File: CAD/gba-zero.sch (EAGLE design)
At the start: 57 parts, among them IC5 APX803, Q2 BSS138, U1 NC7WZ16, U2 LM4875

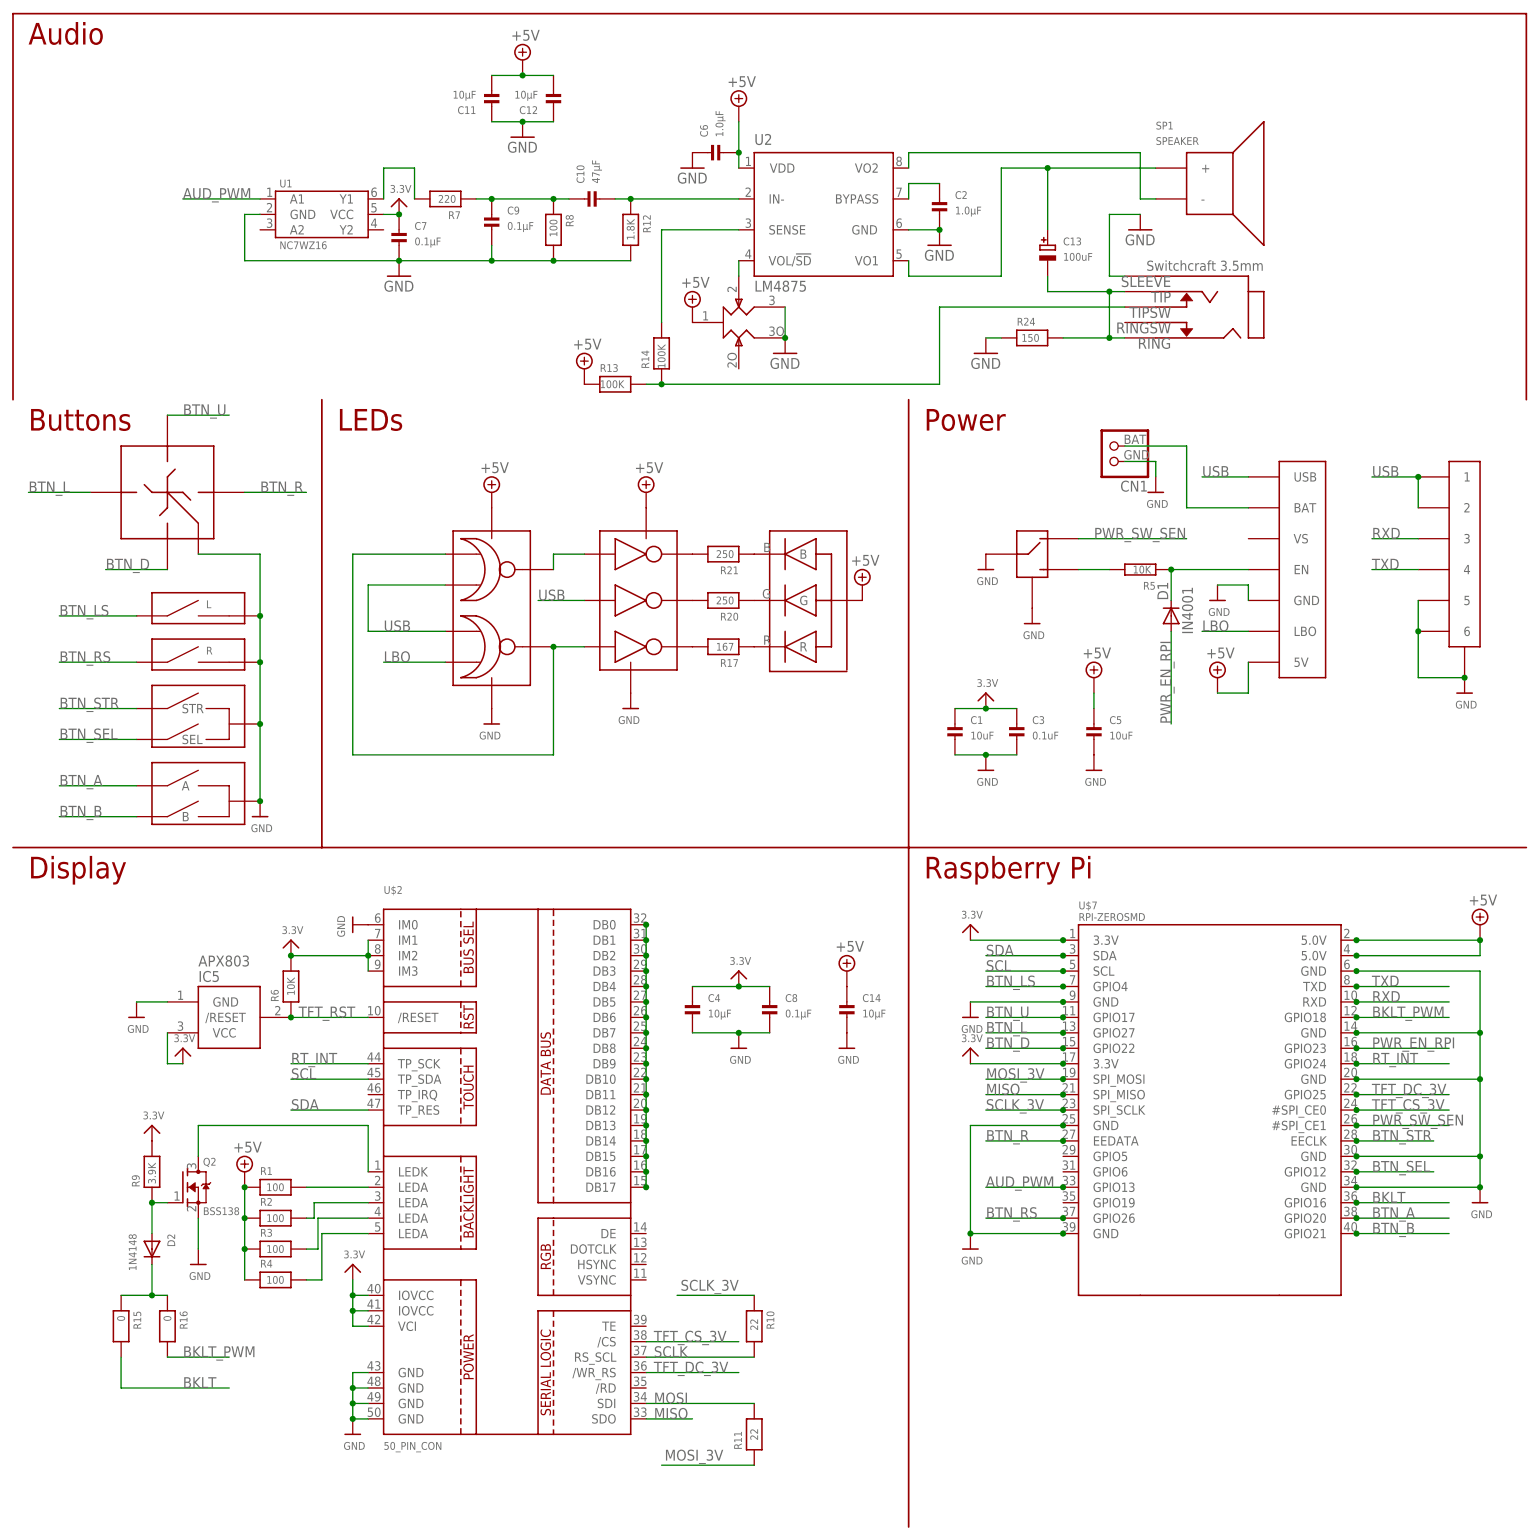
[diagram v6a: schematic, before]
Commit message: Renumbered parts
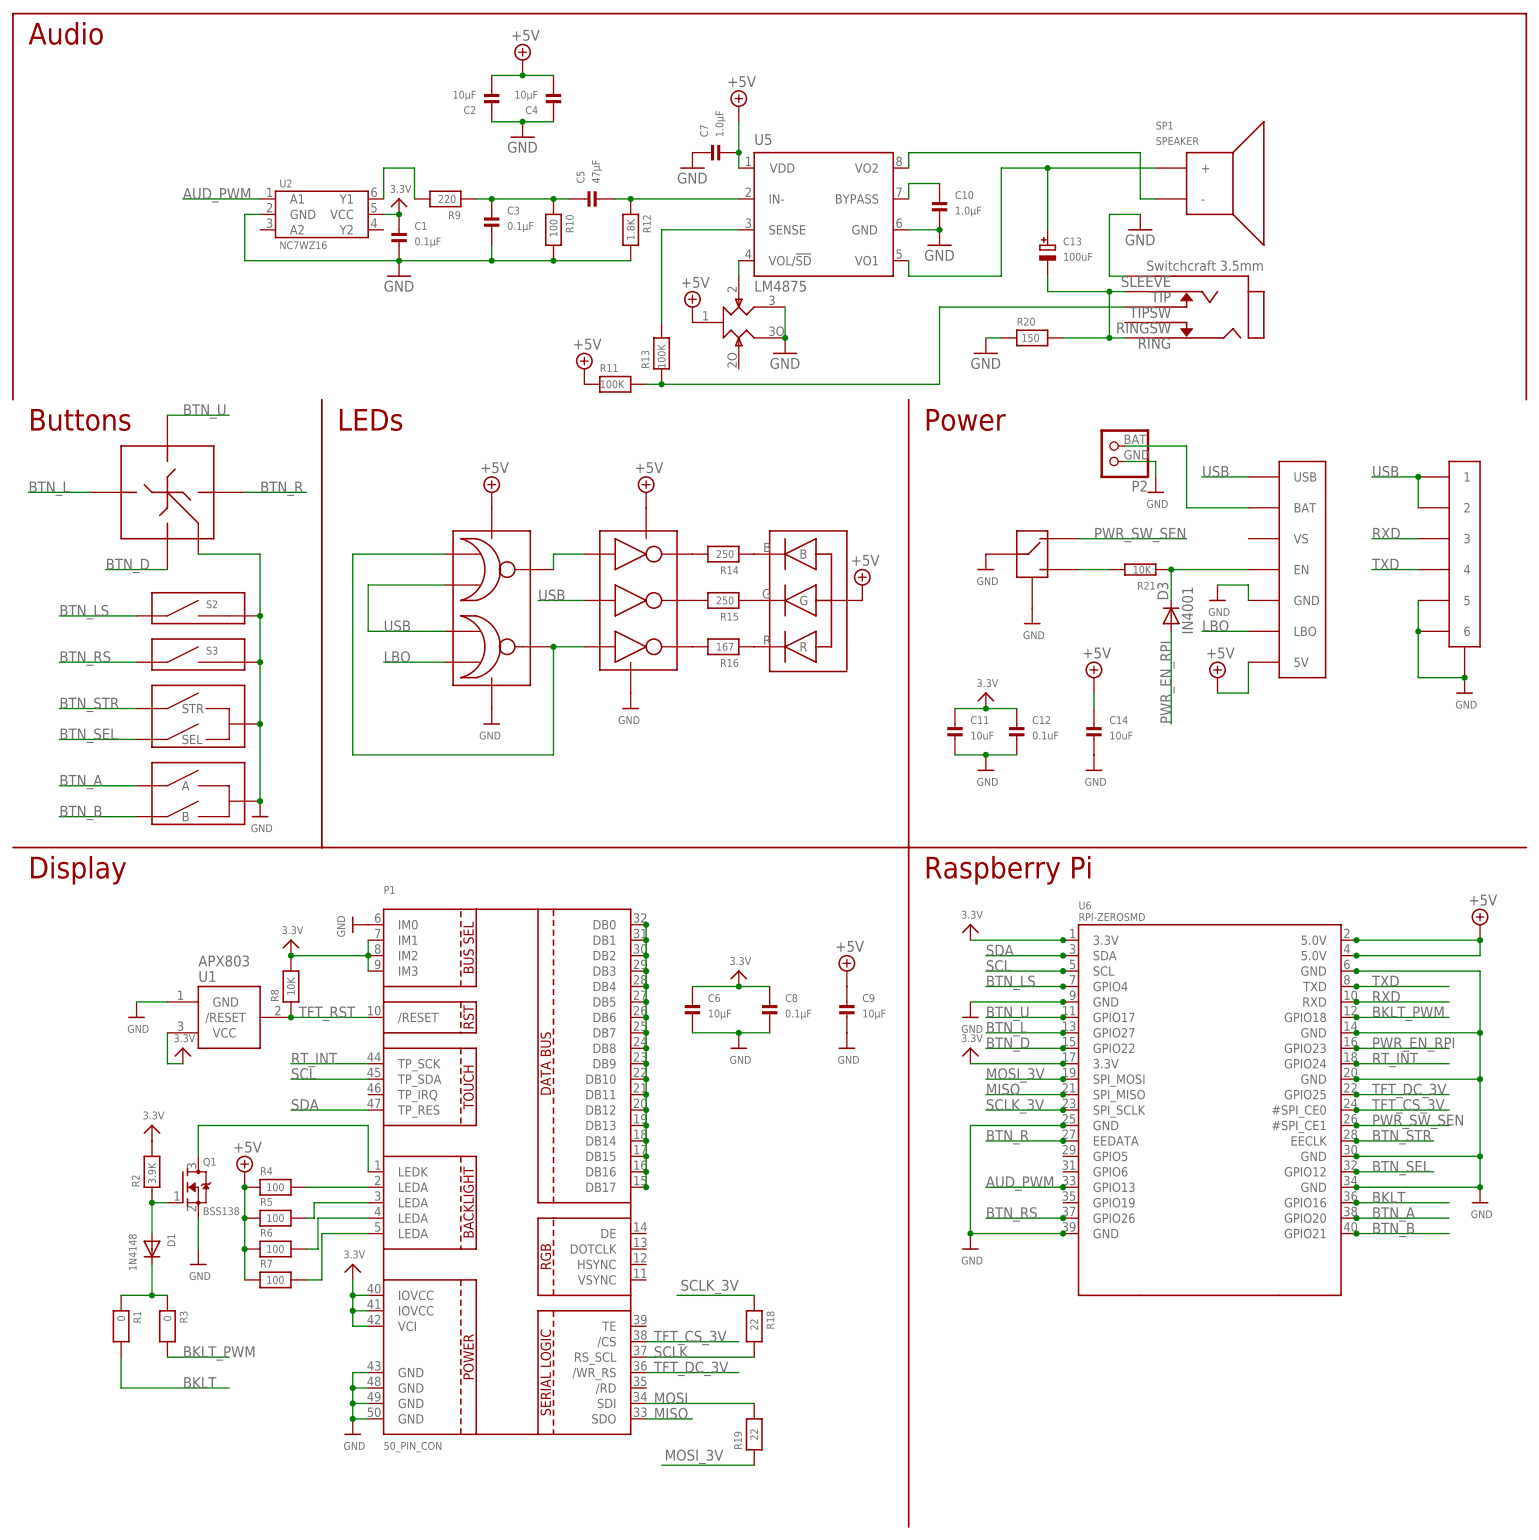
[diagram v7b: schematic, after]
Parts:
- removed IC5: APX803, adafruit:AXP083-SAG
- removed R24: 150, microbuilder:RESISTOR0603
- removed U$17: 10K, gba-zero-parts:RK10J12E0A0A
- removed U$44: LTST-C19HE1WT, gba-zero-parts:LTST-C19HE1WT
- added D3: IN4001, diode:DIODE-D-7.5
- added R18, R19: 22, microbuilder:RESISTOR0805
- added U5: LM4875, gba-zero-parts:LM4875
- C1: value 10uF -> 0.1μF; device microbuilder:CAP_CERAMIC0805 -> microbuilder:CAP_CERAMIC0603
- C10: value 47μF -> 1.0μF
- C11, C14: value 10μF -> 10uF; device microbuilder:CAP_CERAMIC0603 -> microbuilder:CAP_CERAMIC0805
- C12: value 10μF -> 0.1uF; device microbuilder:CAP_CERAMIC0603 -> microbuilder:CAP_CERAMIC0805
- C2, C6: value 1.0μF -> 10μF
- C3: value 0.1uF -> 0.1μF; device microbuilder:CAP_CERAMIC0805 -> microbuilder:CAP_CERAMIC0603
- C5: value 10uF -> 47μF; device microbuilder:CAP_CERAMIC0805 -> microbuilder:CAP_CERAMIC0603
- C7: value 0.1μF -> 1.0μF
- C9: value 0.1μF -> 10μF
- D1: value IN4001 -> 1N4148; device diode:DIODE-D-7.5 -> microbuilder:DIODESOD-323
- D2: value 1N4148 -> LTST-C19HE1WT; device microbuilder:DIODESOD-323 -> gba-zero-parts:LTST-C19HE1WT
- R1, R3: value 100 -> 0; device microbuilder:RESISTOR0805 -> microbuilder:RESISTOR0603
- R10: value 22 -> 100; device microbuilder:RESISTOR0805 -> microbuilder:RESISTOR0603
- R11: value 22 -> 100K; device microbuilder:RESISTOR0805 -> microbuilder:RESISTOR0603
- R14: value 100K -> 250; device microbuilder:RESISTOR0603 -> microbuilder:RESISTOR0805
- R15: value 0 -> 250; device microbuilder:RESISTOR0603 -> microbuilder:RESISTOR0805
- R16: value 0 -> 167; device microbuilder:RESISTOR0603 -> microbuilder:RESISTOR0805
- R17: value 167 -> 10K; device microbuilder:RESISTOR0805 -> gba-zero-parts:RK10J12E0A0A
- R2: value 100 -> 3.9K
- R20: value 250 -> 150; device microbuilder:RESISTOR0805 -> microbuilder:RESISTOR0603
- R21: value 250 -> 10K; device microbuilder:RESISTOR0805 -> resistor:R-EU_0204/7
- R5: value 10K -> 100; device resistor:R-EU_0204/7 -> microbuilder:RESISTOR0805
- R6: value 10K -> 100
- R7: value 220 -> 100; device microbuilder:RESISTOR0603 -> microbuilder:RESISTOR0805
- R8: value 100 -> 10K; device microbuilder:RESISTOR0603 -> microbuilder:RESISTOR0805
- R9: value 3.9K -> 220; device microbuilder:RESISTOR0805 -> microbuilder:RESISTOR0603
- U1: value NC7WZ16 -> APX803; device fairchild:NC7WZ16 -> adafruit:AXP083-SAG
- U2: value LM4875 -> NC7WZ16; device gba-zero-parts:LM4875 -> fairchild:NC7WZ16
- renumbered CN1 to P2, L to S2, Q2 to Q1, R to S3, U$10 to P3, U$11 to S6, U$12 to U7, U$16 to J1, U$18 to S4, U$2 to P1, U$20 to S5, U$3 to S1, U$42 to U3, U$43 to U4, U$7 to U6
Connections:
- net +5V: now also C2.P$2, C4.P$2, C7.P$2, C9.P$1, D2.VCC, R11.1, R17.1, R5.1, R6.1, R7.1, U5.VDD; no longer C11.P$2, C12.P$2, C5.P$1, C6.P$2, R1.1, R13.1, R2.1, R3.1, U$17.1, U$44.VCC, U2.VDD
- net 3.3V: now also C11.P$1, C12.P$1, C6.P$1, R2.2, R8.2, U2.VCC; no longer C3.P$1, C4.P$1, C7.P$1, IC5.VCC, R6.2, R9.2
- net AUD_PWM: now also U2.A1; no longer U1.A1
- net BKLT: now also R1.2; no longer R15.2
- net BKLT_PWM: now also R3.2; no longer R16.2
- net BYPASS: now also C10.P$1, U5.BYPASS; no longer C2.P$1, U2.BYPASS
- net GND: now also C10.P$2, C11.P$2, C12.P$2, C2.P$1, C4.P$1, C6.P$2, C7.P$1, R10.2, R17.3, R17.3O, R20.1, U2.GND, U5.GND@; no longer C11.P$1, C12.P$1, C2.P$2, C4.P$2, C5.P$2, C6.P$1, C7.P$2, IC5.GND, R24.1, R8.2, U$17.3, U$17.3O, U2.GND@
- net IN-: now also C5.P$2, U5.IN-; no longer C10.P$2, U2.IN-
- net MOSI: now also R19.2; no longer R11.2
- net MOSI_3V: now also R19.1; no longer R11.1
- net N$10: now also R4.2; no longer R1.2
- net N$11: now also R15.2; no longer R20.2
- net N$12: now also D2.G, R15.1; no longer R20.1, U$44.G
- net N$13: now also R14.2; no longer R21.2
- net N$14: now also D2.B, R14.1; no longer R21.1, U$44.B
- net N$17: now also R21.2; no longer R5.2
- net N$18: now also D3.C, R21.1; no longer D1.C, R5.1
- net N$2: now also R7.2; no longer R4.2
- net N$20: now also R9.2, U2.Y1; no longer R7.2, U1.Y1
- net N$21: now also C3.P$1, C5.P$1, R10.1, R9.1; no longer C10.P$1, C9.P$1, R7.1, R8.1
- net N$22: now also R11.2, R13.1; no longer R13.2, R14.1
- net N$3: now also R6.2; no longer R3.2
- net N$4: now also R5.2; no longer R2.2
- net N$5: now also R16.2; no longer R17.2
- net N$6: now also D1.C, R1.1, R3.1; no longer D2.C, R15.1, R16.1
- net N$7: now also D1.A, R2.1; no longer D2.A, R9.1
- net N$8: now also D2.R, R16.1; no longer R17.1, U$44.R
- net PWR_EN_RPI: now also D3.A; no longer D1.A
- net RING: now also R20.2; no longer R24.2
- net SCLK: now also R18.2; no longer R10.2
- net SCLK_3V: now also R18.1; no longer R10.1
- net SENSE: now also R13.2, U5.SENSE; no longer R14.2, U2.SENSE
- net TFT_RST: now also R8.1, U1./RESET; no longer IC5./RESET, R6.1
- net VO1: now also U5.VO1; no longer U2.VO1
- net VO2: now also U5.VO2; no longer U2.VO2
- net VOL/SD: now also R17.2, U5.VOL/!SD; no longer U$17.2, U2.VOL/!SD
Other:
- moved on the sheet: C1, C10, C11, C12, C14, C2, C3, C4, C5, C6, C7, C9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

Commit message: Fixed u vs. μ Removed jack outline from bPlace Fixed the date on the silk
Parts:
- C11, C14: value 10uF -> 10μF
- C12: value 0.1uF -> 0.1μF
- C13: value 100uF -> 100μF
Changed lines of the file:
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@@
 <part name="GND2" library="microbuilder" deviceset="GND" device=""/>
 <part name="GND19" library="microbuilder" deviceset="GND" device=""/>
-<part name="C12" library="microbuilder" deviceset="CAP_CERAMIC" device="0805" value="0.1uF"/>
-<part name="C11" library="microbuilder" deviceset="CAP_CERAMIC" device="0805" value="10uF"/>
-<part name="C14" library="microbuilder" deviceset="CAP_CERAMIC" device="0805" value="10uF"/>
+<part name="C12" library="microbuilder" deviceset="CAP_CERAMIC" device="0805" value="0.1μF"/>
+<part name="C11" library="microbuilder" deviceset="CAP_CERAMIC" device="0805" value="10μF"/>
+<part name="C14" library="microbuilder" deviceset="CAP_CERAMIC" device="0805" value="10μF"/>
 <part name="SUPPLY10" library="supply2" deviceset="+5V" device=""/>
 <part name="GND21" library="microbuilder" deviceset="GND" device=""/>
@@
 <part name="C2" library="microbuilder" deviceset="CAP_CERAMIC" device="0603" value="10μF"/>
 <part name="C4" library="microbuilder" deviceset="CAP_CERAMIC" device="0603" value="10μF"/>
-<part name="C13" library="microbuilder" deviceset="CAP_ELECTROLYTIC" device="PANASONIC_D" value="100uF"/>
+<part name="C13" library="microbuilder" deviceset="CAP_ELECTROLYTIC" device="PANASONIC_D" value="100μF"/>
 <part name="U5" library="gba-zero-parts" deviceset="LM4875" device=""/>
 <part name="GND14" library="SparkFun-Aesthetics" deviceset="GND" device=""/>
